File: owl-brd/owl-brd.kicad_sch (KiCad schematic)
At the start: 53 parts, among them J1 JST, J10 JST, J11 JST, J12 JST, J13 Screw_Terminal_01x02, J14 1x4 Socket, J15 CLTCH1, J16 CLTCH2, J17 CLTCH3, J18 CLTCH4, J19 CLTCH5, J2 JST, J20 CLTCH6, J21 CLTCH7, J22 CLTCH1, J23 Conn_01x03, J24 Conn_01x03, J25 Conn_01x03, J26 Conn_01x03, J27 Screw_Terminal_01x02, J28 JST, J29 Ext Power, J3 JST, J30 Power/UART, J4 JST, J5 JST, J6 JST, J7 JST, J8 JST, J9 JST, Q9 IRLB8721PBF, U1 Pico, U2 L7805CV, U3 TMC2209_SILENTSTEPSTICK, U4 TMC2209_SILENTSTEPSTICK, U5 TMC2209_SILENTSTEPSTICK, U6 TCA9548APWR, U7 74HC238, U8 ULN2803A

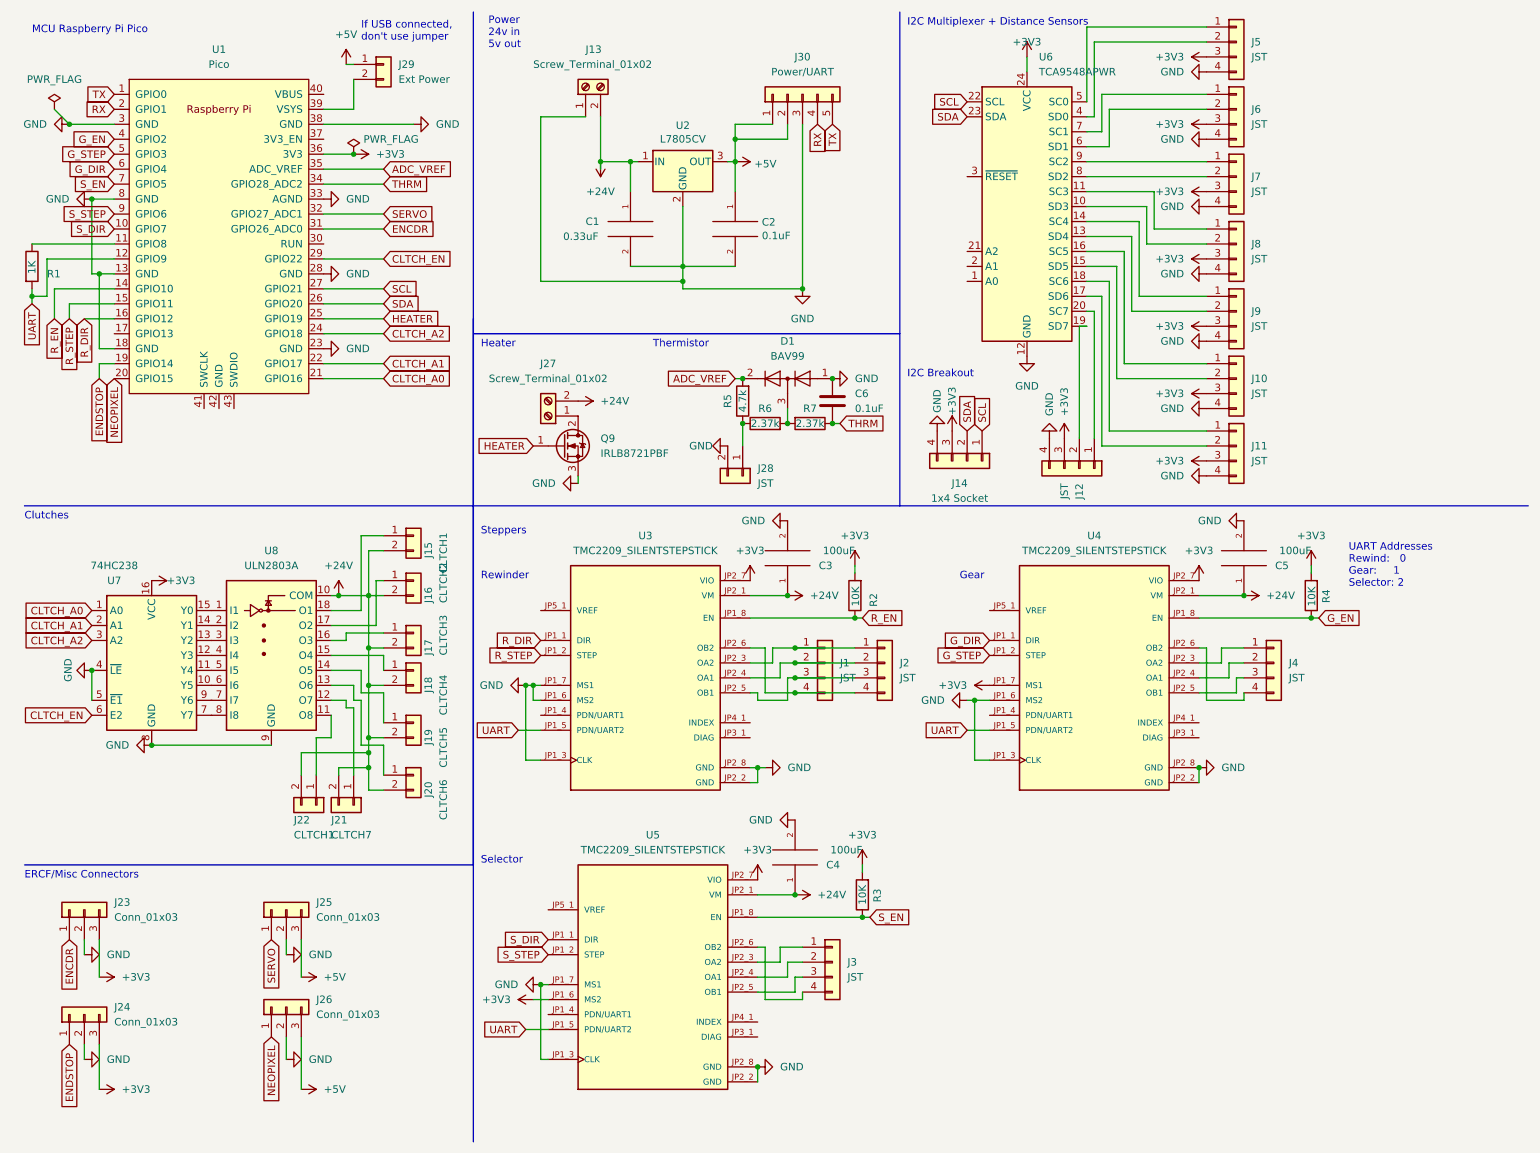
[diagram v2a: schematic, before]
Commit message: Revision 1.0.1 - Removed 5v on UART pins (output isn't enough for pi) - Notes/minor cleanup for production
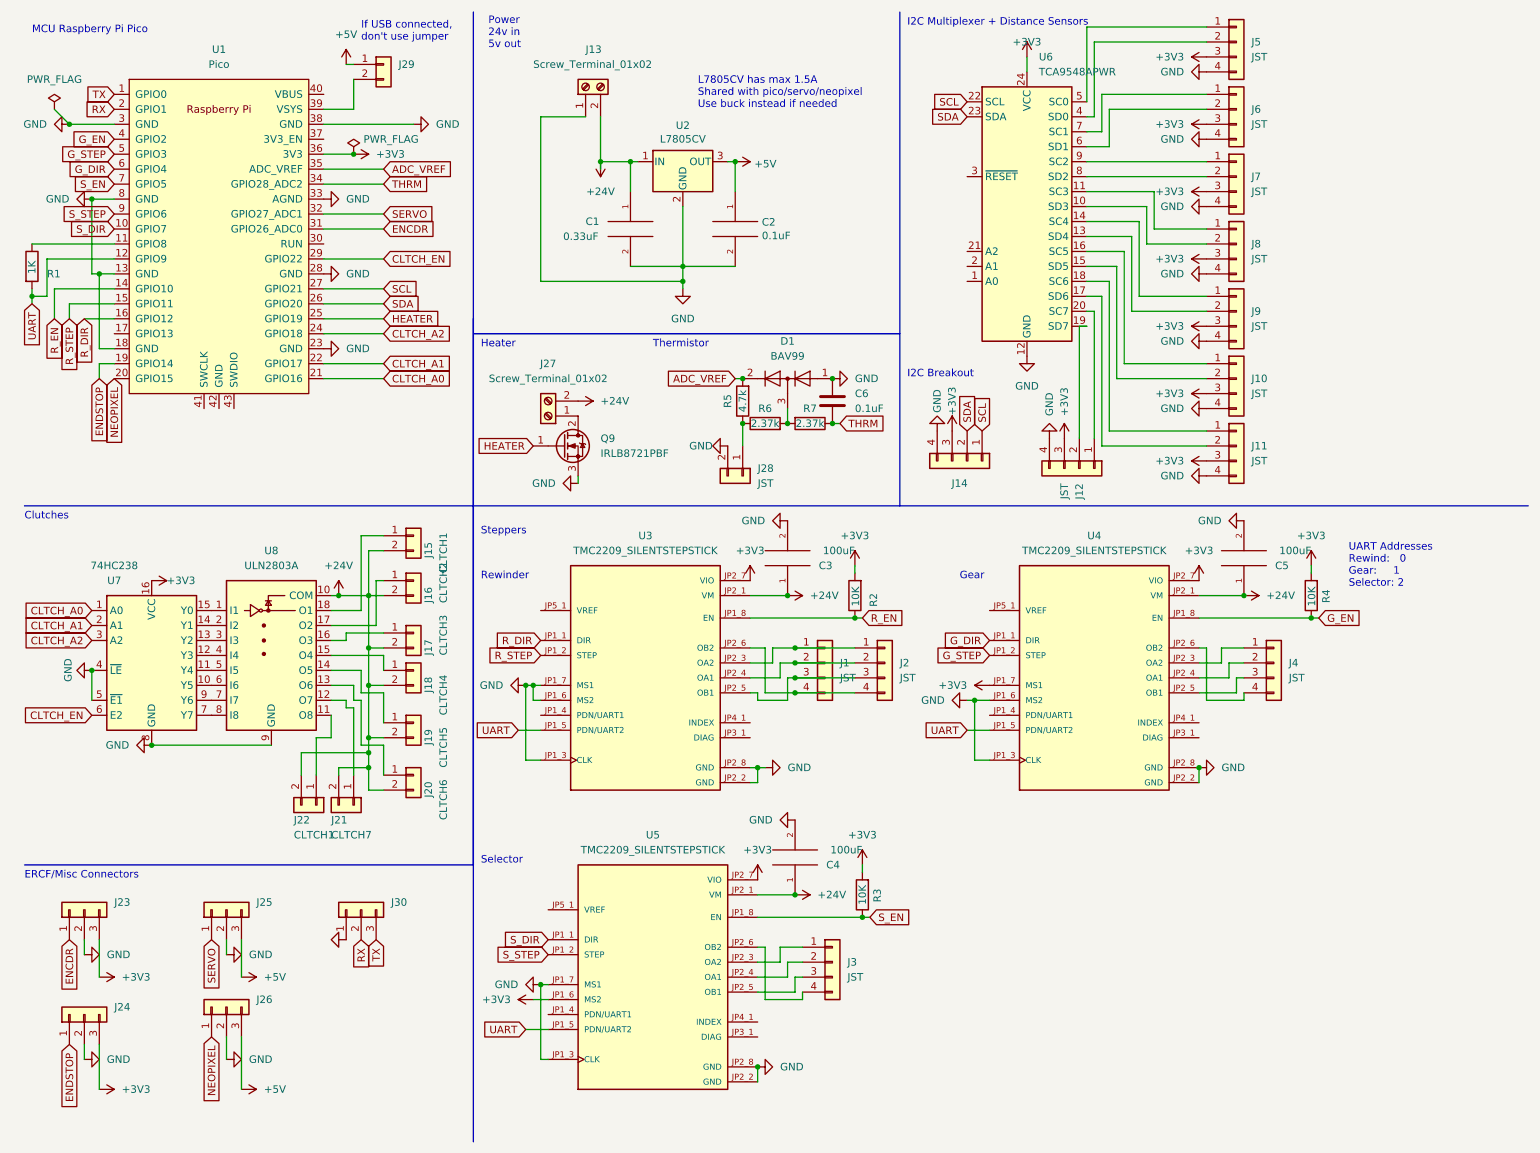
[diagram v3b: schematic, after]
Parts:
- J14: value 1x4 Socket -> (none); footprint Connector_PinSocket_2.54mm:PinSocket_1x04_P2.54mm_Vertical -> (none)
- J23, J24, J25, J26: value Conn_01x03 -> (none)
- J29: value Ext Power -> (none); footprint Connector_PinSocket_2.54mm:PinSocket_1x02_P2.54mm_Vertical -> (none)
- J30: value Power/UART -> (none); footprint Connector_PinSocket_2.54mm:PinSocket_1x05_P2.54mm_Vertical -> (none); symbol Connector_Generic:Conn_01x05 -> Connector_Generic:Conn_01x03
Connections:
- net +5V: no longer J30.1 (Pin_1), J30.2 (Pin_2)
- net GND: now also J30.1 (Pin_1); no longer J30.3 (Pin_3)
- net RX: now also J30.2 (Pin_2); no longer J30.4 (Pin_4)
- net TX: now also J30.3 (Pin_3); no longer J30.5 (Pin_5)
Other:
- note added: "L7805CV has max 1.5A Shared with pico/servo/neopixel Use buck instead if needed"
- moved on the sheet: J25, J26
